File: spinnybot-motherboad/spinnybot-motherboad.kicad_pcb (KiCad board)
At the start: 2 copper layers, 76.2 x 76 mm, 64 parts, among them J1 +12V, J11 CAP SWITCH, J12 LEDSTRIP3, J13 LEDSTRIP2, J14 LEDSTRIP3, J2 LEDSTRIP1, J3 LEDSTRIP1, J4 LEDSTRIP2, J5 GND, J6 MOTOR2, J7 MOTOR3, J8 MOTOR1, J9 CAP SWITCH, Q1 SISA96DN, Q2 SISA96DN, Q3 BC846, Q4 NPN, Q5 PNP, U1 LM1117-3.3, U2 XBP9B-DMWT-002, U3 SN74LVC1G74, U4 ICM-20649, U5 ESP32-DEVKITC-32D, U6 SN74AHCT541DW, U7 SN74AHCT541DW

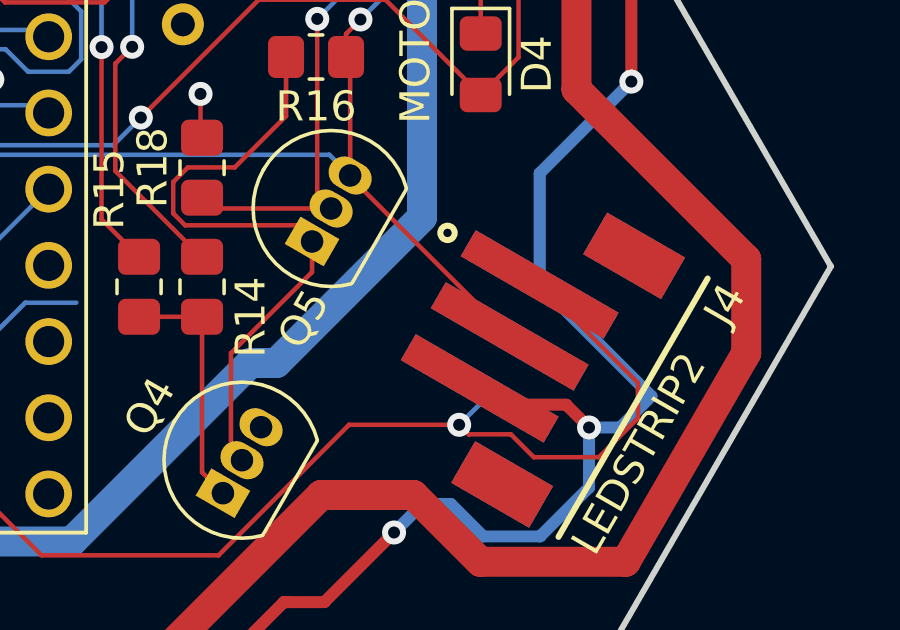
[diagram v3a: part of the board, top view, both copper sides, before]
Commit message: added PDF schematic and fixed a routing error
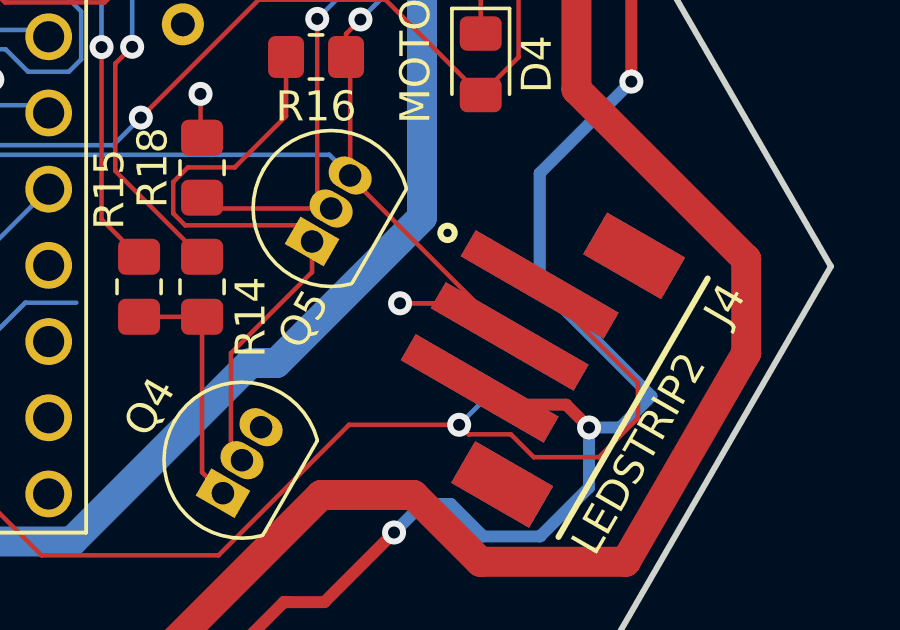
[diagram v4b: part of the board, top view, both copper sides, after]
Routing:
- net +5V: track 235.8 -> 244.0 mm, vias 11 -> 12
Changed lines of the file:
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@@
     (fp_line (start 4.975 2.5) (end -4.975 2.5) (layer "F.Fab") (width 0.2))
     (pad "1" smd rect (at -2 2.25 240) (locked) (size 1 5.5) (layers "F.Cu" "F.Paste" "F.Mask")
-      (net 12 "/LEDSTRIP2_DATA_5V") (pinfunction "Pin_1") (pintype "passive"))
+      (net 12 "/LEDSTRIP2_DATA_5V") (pinfunction "Pin_1"))
     (pad "2" smd rect (at 0 2.25 240) (locked) (size 1 5.5) (layers "F.Cu" "F.Paste" "F.Mask")
-      (net 3 "+5V") (pinfunction "Pin_2") (pintype "passive"))
+      (net 3 "+5V") (pinfunction "Pin_2"))
     (pad "3" smd rect (at 2 2.25 240) (locked) (size 1 5.5) (layers "F.Cu" "F.Paste" "F.Mask")
-      (net 9 "/LEDSTRIP_GND") (pinfunction "Pin_3") (pintype "passive"))
+      (net 9 "/LEDSTRIP_GND") (pinfunction "Pin_3"))
     (pad "4" smd rect (at 4.4 0 240) (locked) (size 1.6 3) (layers "F.Cu" "F.Paste" "F.Mask"))
     (pad "5" smd rect (at -4.4 0 240) (locked) (size 1.6 3) (layers "F.Cu" "F.Paste" "F.Mask"))
@@
   (segment (start 171.83 68.41) (end 172.777142 69.357142) (width 0.1524) (layer "F.Cu") (net 3))
   (segment (start 194.276769 113.540148) (end 194.276769 113.58662) (width 0.1524) (layer "F.Cu") (net 3))
+  (segment (start 198.490149 117.8) (end 199.594046 118.903897) (width 0.1524) (layer "F.Cu") (net 3))
   (segment (start 194.14 108.82) (end 194.62 108.34) (width 0.1524) (layer "F.Cu") (net 3))
   (segment (start 201.85 91.35) (end 201.85 90.51) (width 0.1524) (layer "F.Cu") (net 3))
   (segment (start 200.555 92.645) (end 201.85 91.35) (width 0.1524) (layer "F.Cu") (net 3))
+  (segment (start 195.94 117.8) (end 198.490149 117.8) (width 0.1524) (layer "F.Cu") (net 3))
   (segment (start 156.25 79.11) (end 159.59 75.77) (width 0.1524) (layer "F.Cu") (net 3))
   (segment (start 163.58 75.77) (end 163.6 75.79) (width 0.1524) (layer "F.Cu") (net 3))
   (segment (start 194.276769 113.540148) (end 194.276769 109.726769) (width 0.1524) (layer "F.Cu") (net 3))
+  (via (at 195.94 117.8) (size 0.8) (drill 0.4) (layers "F.Cu" "B.Cu") (free) (net 3))
   (via (at 150.73 112.28) (size 0.8) (drill 0.4) (layers "F.Cu" "B.Cu") (net 3))
   (via (at 155.17 79.11) (size 0.8) (drill 0.4) (layers "F.Cu" "B.Cu") (net 3))
@@
   (segment (start 163.92 121.562659) (end 163.92 119.2) (width 0.1524) (layer "B.Cu") (net 3))
   (segment (start 176.091114 116.684187) (end 176.797113 116.684187) (width 0.1524) (layer "B.Cu") (net 3))
+  (segment (start 198.490149 117.8) (end 195.94 117.8) (width 0.1524) (layer "B.Cu") (net 3))
+  (segment (start 199.594046 118.903897) (end 198.490149 117.8) (width 0.1524) (layer "B.Cu") (net 3))
   (segment (start 196.5225 89.51) (end 197.0525 88.98) (width 0.1524) (layer "B.Cu") (net 3))
   (segment (start 163.92 119.2) (end 165.3 117.82) (width 0.1524) (layer "B.Cu") (net 3))

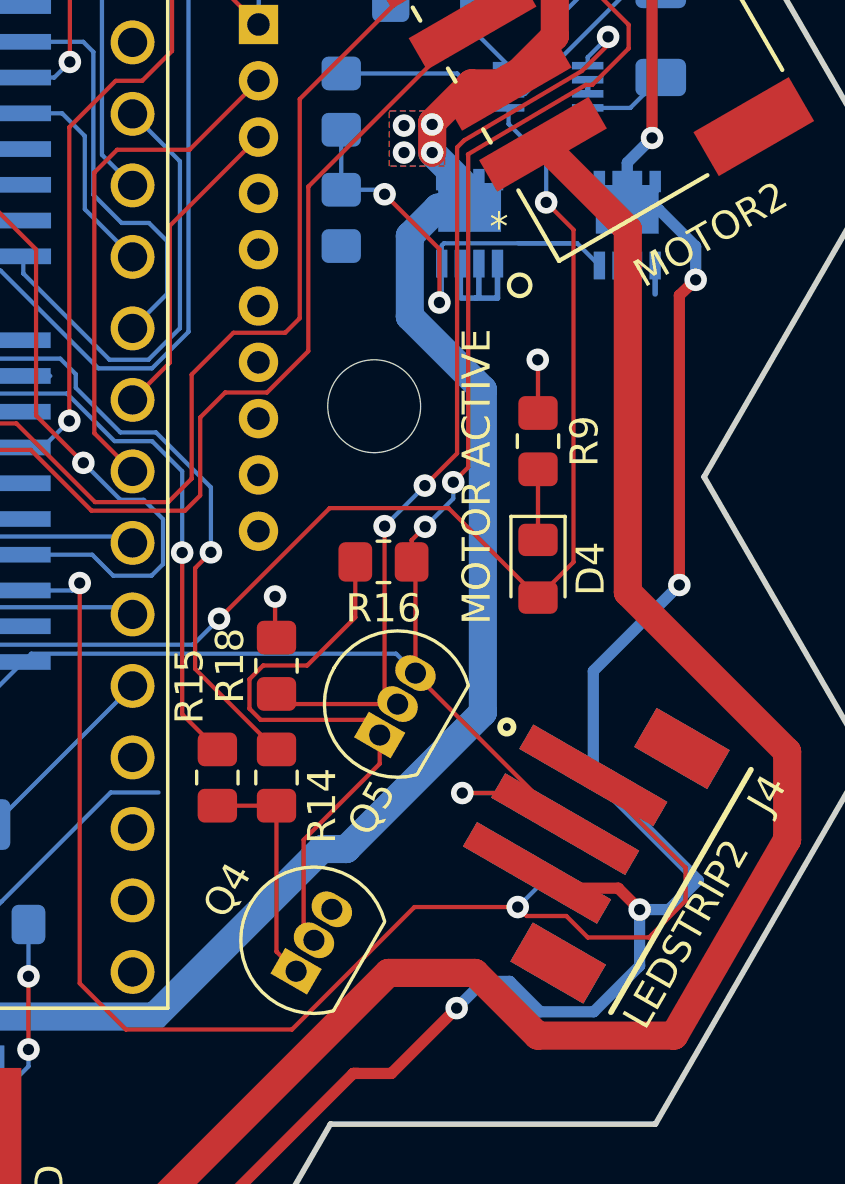
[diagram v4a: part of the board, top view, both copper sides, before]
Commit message: Replaced transistor symbols and footprints with correct ones.
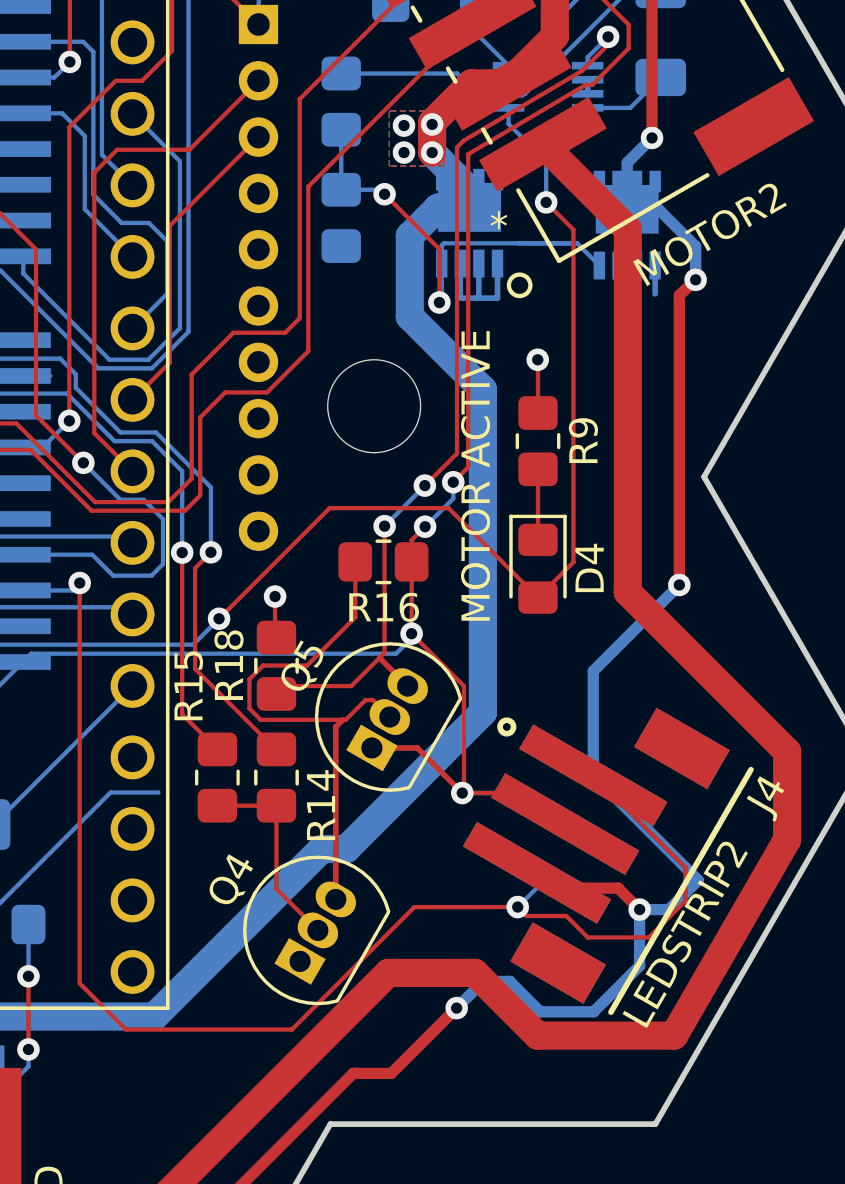
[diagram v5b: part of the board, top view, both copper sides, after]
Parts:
- Q4: value NPN -> 2N3904
- Q5: value PNP -> 2N3906
- moved Q5 0.54 mm to (192.7, 116.2)
- moved Q4 0.38 mm to (190.2, 123.8)
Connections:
- Q4 pad 1: Net-(Q4-Pad1) -> GND
- Q4 pad 2: Net-(Q4-Pad2) -> Net-(R14-Pad1)
- Q4 pad 3: GND -> Net-(Q4-Pad3)
- Q5 pad 1: Net-(Q4-Pad2) -> +5V
- Q5 pad 2: /POWER_TOGGLE -> Net-(Q4-Pad3)
- Q5 pad 3: +5V -> /POWER_TOGGLE
- R14 pad 1: Net-(Q4-Pad1) -> Net-(R14-Pad1)
- R15 pad 1: Net-(Q4-Pad1) -> Net-(R14-Pad1)
- R16 pad 2: Net-(Q4-Pad2) -> Net-(Q4-Pad3)
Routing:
- net Net-(Q4-Pad2): track 21.3 -> 0.00 mm
- net Net-(Q4-Pad3): track 0.00 -> 19.9 mm
- net Net-(Q4-Pad1): track 8.27 -> 0.00 mm
- net Net-(R14-Pad1): track 0.00 -> 7.14 mm
- net +5V: track 244.0 -> 245.4 mm, vias 12 -> 13
- net /POWER_TOGGLE: track 33.9 -> 33.0 mm

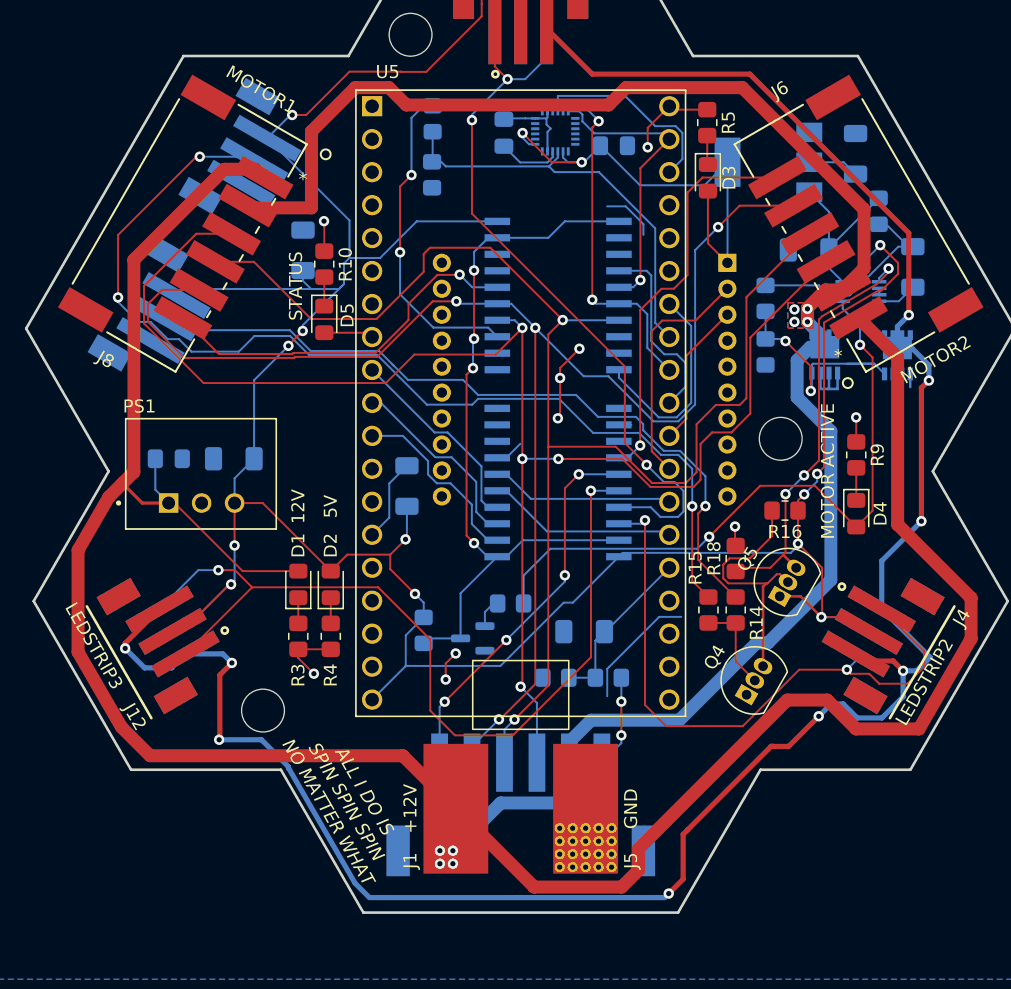
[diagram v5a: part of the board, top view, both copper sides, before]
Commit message: fixed some reference designators so the layout isn't broken
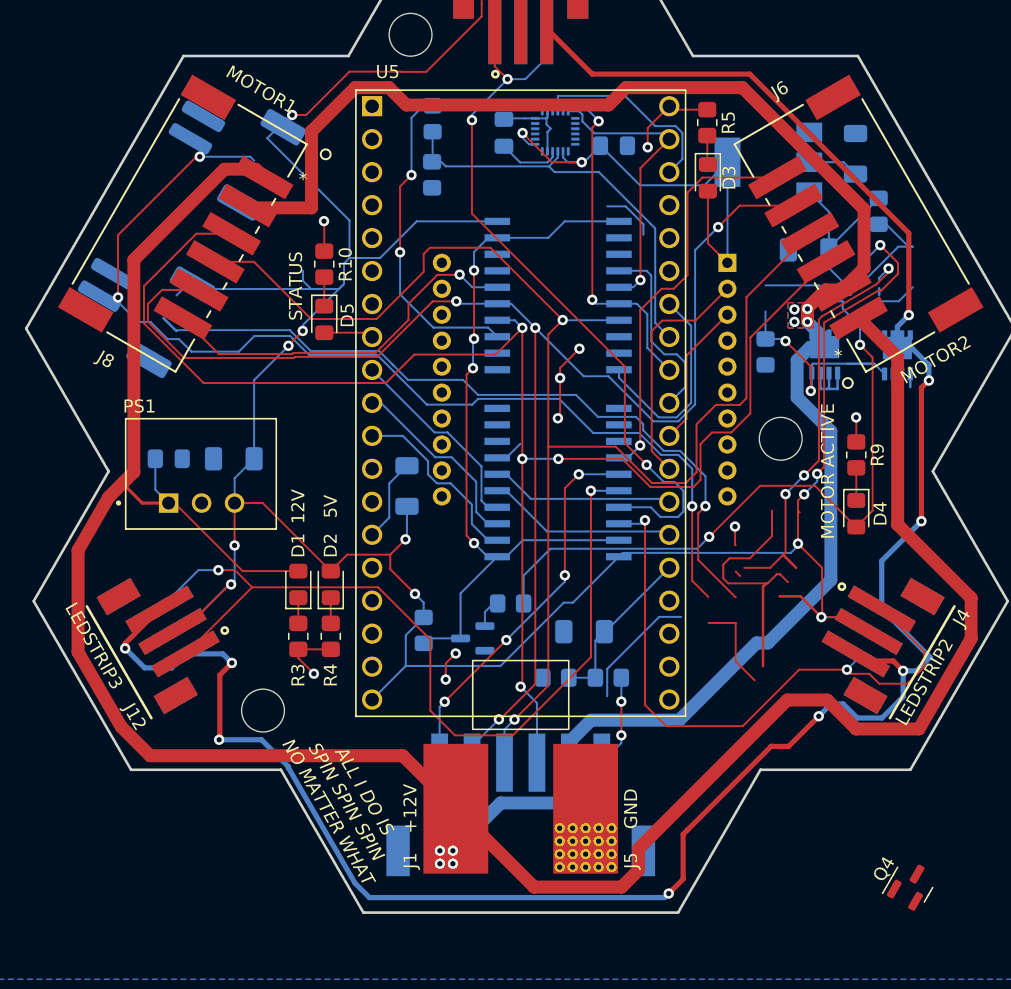
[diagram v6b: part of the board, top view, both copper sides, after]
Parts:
- removed C10, C6: 10u, Capacitor_SMD:C_1206_3216Metric_Pad1.33x1.80mm_HandSolder
- removed Q5: 2N3906, Package_TO_SOT_THT:TO-92_Inline
- removed R14, R15, R16, R18: 1K, Resistor_SMD:R_0805_2012Metric_Pad1.20x1.40mm_HandSolder
- removed R8: 200, Resistor_SMD:R_0805_2012Metric_Pad1.20x1.40mm_HandSolder
- removed U3: SN74LVC1G74, SN74LVC1G74DCUR:SOP50P310X90-8N
- J11: value CAP SWITCH -> POWER SW2; footprint B3B-PH-SM4:JST_B3B-PH-SM4-TB(LF)(SN) -> Connector_JST:JST_PH_S2B-PH-SM4-TB_1x02-1MP_P2.00mm_Horizontal
- J9: value CAP SWITCH -> POWER SW1; footprint B3B-PH-SM4:JST_B3B-PH-SM4-TB(LF)(SN) -> Connector_JST:JST_PH_S2B-PH-SM4-TB_1x02-1MP_P2.00mm_Horizontal
- Q4: value 2N3904 -> Q_NMOS_DGS; footprint Package_TO_SOT_THT:TO-92_Inline -> Package_TO_SOT_SMD:SOT-23
- R6: value 1K -> 1k
- R7: value 10K -> 2k
- R9: value 1K -> 220
- U2: value XBP9B-DMWT-002 -> XBP9B-DMWTB002; footprint XBee_PRO900HP_S3B:DIP2200W51P200L3294H279Q20P -> XBP9-DMWTB002-XBEE-PRO-900HP:DIP2200W51P200L3294H279Q20P
- moved Q4 19.4 mm to (202.8, 138.4)
- renumbered G*** to #LOGO1, REF** to #LOGO2
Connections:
- net /XBEE_RX renamed /MCU and Buffers/XBEE_RX
- net /XBEE_TX renamed /MCU and Buffers/XBEE_TX
- C5 pad 1: +5V -> GND
- C5 pad 2: GND -> /POWER_ON
- D4 pad 2: /DFF_Q -> +5V
- J11 pad 1: +5V -> GND
- J11 pad 2: /SW2 -> Net-(J9-Pad2)
- J9 pad 1: +5V -> GND
- J9 pad 2: /SW1 -> Net-(J9-Pad2)
- Q1 pad 4: /FET_G -> /POWER_ON
- Q1 pad 5: /LEDSTRIP_GND -> /LEDSTRIP_GROUND
- Q2 pad 4: /FET_G -> /POWER_ON
- Q4 pad 1: GND -> Net-(Q4-Pad1)
- Q4 pad 2: Net-(R14-Pad1) -> /POWER_ON
- Q4 pad 3: Net-(Q4-Pad3) -> GND
- R17 pad 2: /DFF_Q -> /POWER_ON
- R6 pad 2: /DFF_RESET -> Net-(J9-Pad2)
- R7 pad 1: GND -> Net-(J9-Pad2)
- R7 pad 2: /FET_G -> /POWER_ON
- R9 pad 1: GND -> Net-(Q4-Pad1)
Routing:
- net (no net): track 0.00 -> 112.8 mm, vias 0 -> 4
- net Net-(J9-Pad2): track 0.00 -> 89.9 mm, vias 0 -> 3
- net /SW2: track 79.6 -> 0.00 mm, vias 3 -> 0
- net /SW1: track 59.4 -> 0.00 mm, vias 1 -> 0
- net +5V: track 245.4 -> 302.7 mm, vias 13 -> 15
- net /DFF_Q: track 57.3 -> 0.00 mm, vias 2 -> 0
- net /POWER_TOGGLE: track 33.0 -> 0.00 mm, vias 3 -> 0
- net Net-(Q4-Pad3): track 19.9 -> 0.00 mm
- net /POWER_ON: track 0.00 -> 18.5 mm, vias 0 -> 2
- net /FET_G: track 18.5 -> 0.00 mm, vias 2 -> 0
- net /DFF_RESET: track 10.3 -> 0.00 mm
- net Net-(R14-Pad1): track 7.14 -> 0.00 mm
- net GND: track 82.6 -> 87.9 mm
- net Net-(Q4-Pad1): track 0.00 -> 1.89 mm
- net /DFF_QN: track 0.50 -> 0.00 mm
